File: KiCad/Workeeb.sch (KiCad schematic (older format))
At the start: 103 parts

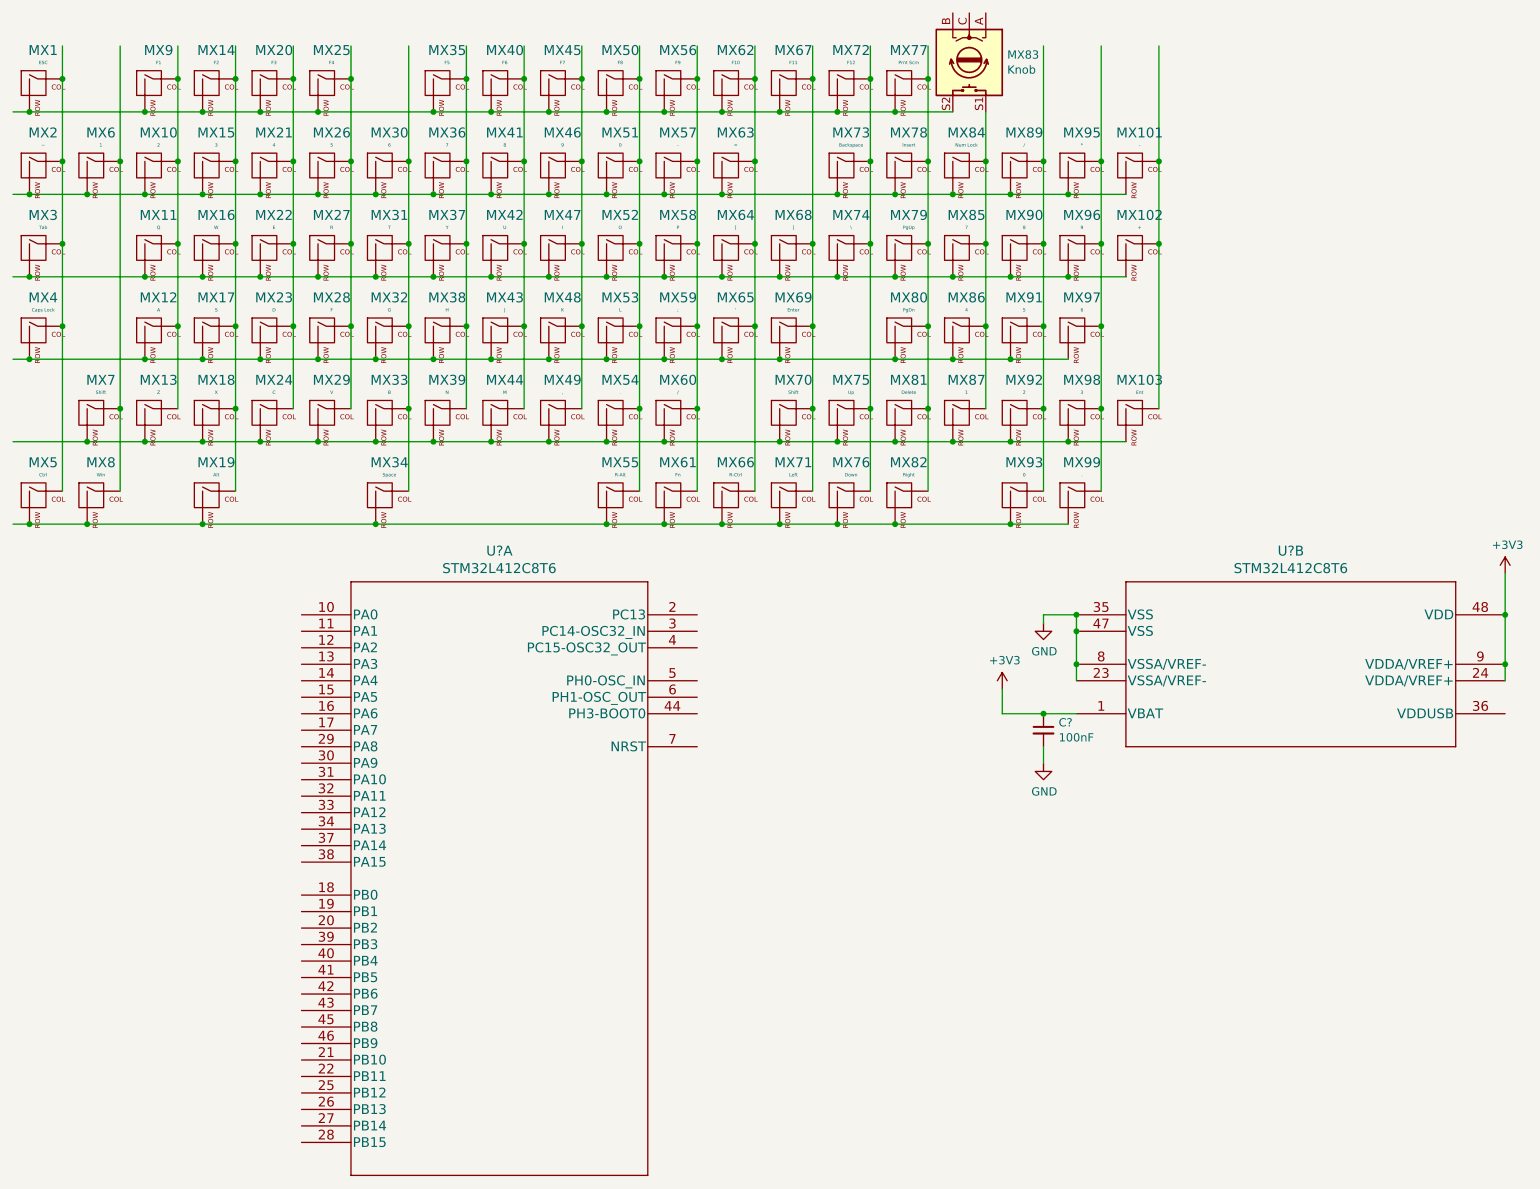
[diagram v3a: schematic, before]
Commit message: Place some things and rename some stuff
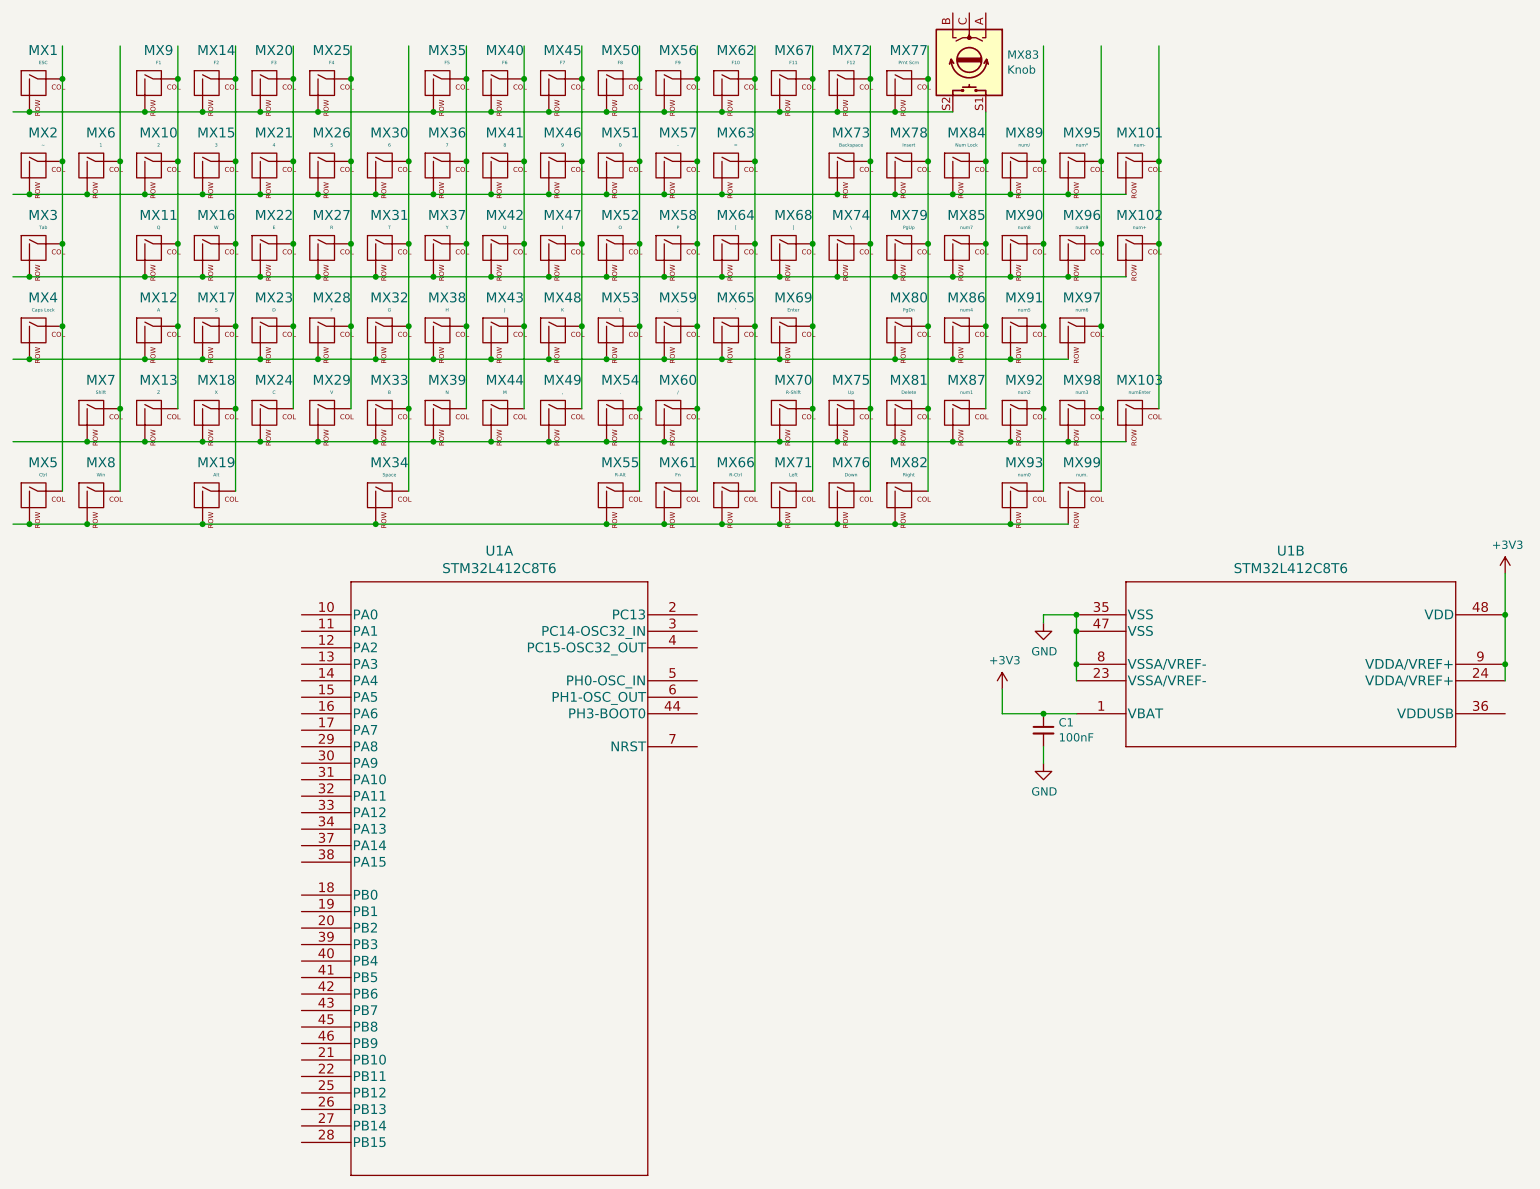
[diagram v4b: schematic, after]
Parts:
- C1: renamed from C?; footprint (none) -> Capacitor_SMD:C_0805_2012Metric
- MX101: value - -> num-
- MX102: value + -> num+
- MX103: value Ent -> numEnter
- MX70: value Shift -> R-Shift
- MX85: value 7 -> num7
- MX86: value 4 -> num4
- MX87: value 1 -> num1
- MX89: value / -> num/
- MX90: value 8 -> num8
- MX91: value 5 -> num5
- MX92: value 2 -> num2
- MX93: value 0 -> num0
- MX95: value * -> num*
- MX96: value 9 -> num9
- MX97: value 6 -> num6
- MX98: value 3 -> num3
- MX99: value . -> num.
- U1: renamed from U?; footprint LQFP-48 -> STM32L412C8T6:STM32L412C8T6
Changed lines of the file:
@@
-$EndComp
-$Comp
-L Workeeb-rescue:MX-NoLED-MX_Alps_Hybrid MX70
-U 1 1 61A3D951
-P 5450 3050
-F 0 "MX70" H 5483 3273 60  0000 C CNN
-F 1 "Shift" H 5483 3199 20  0000 C CNN
-F 2 "MX_Only:MXOnly-1.75U-NoLED" H 4825 3025 60  0001 C CNN
-F 3 "" H 4825 3025 60  0001 C CNN
-	1    5450 3050
-	1    0    0    -1
 $EndComp
 $Comp
@@
 P 6500 2050
 F 0 "MX85" H 6533 2273 60  0000 C CNN
-F 1 "7" H 6533 2199 20  0000 C CNN
+F 1 "num7" H 6533 2199 20  0000 C CNN
 F 2 "MX_Only:MXOnly-1U-NoLED" H 5875 2025 60  0001 C CNN
 F 3 "" H 5875 2025 60  0001 C CNN
 	1    6500 2050
-	1    0    0    -1
-$EndComp
-$Comp
-L Workeeb-rescue:MX-NoLED-MX_Alps_Hybrid MX86
-U 1 1 61A4EEF6
-P 6500 2550
-F 0 "MX86" H 6533 2773 60  0000 C CNN
-F 1 "4" H 6533 2699 20  0000 C CNN
-F 2 "MX_Only:MXOnly-1U-NoLED" H 5875 2525 60  0001 C CNN
-F 3 "" H 5875 2525 60  0001 C CNN
-	1    6500 2550
 	1    0    0    -1
 $EndComp
@@
 P 6500 3050
 F 0 "MX87" H 6533 3273 60  0000 C CNN
-F 1 "1" H 6533 3199 20  0000 C CNN
+F 1 "num1" H 6533 3199 20  0000 C CNN
 F 2 "MX_Only:MXOnly-1U-NoLED" H 5875 3025 60  0001 C CNN
 F 3 "" H 5875 3025 60  0001 C CNN
@@
 P 6850 1550
 F 0 "MX89" H 6883 1773 60  0000 C CNN
-F 1 "/" H 6883 1699 20  0000 C CNN
+F 1 "num/" H 6883 1699 20  0000 C CNN
 F 2 "MX_Only:MXOnly-1U-NoLED" H 6225 1525 60  0001 C CNN
 F 3 "" H 6225 1525 60  0001 C CNN
@@
 P 6850 2050
 F 0 "MX90" H 6883 2273 60  0000 C CNN
-F 1 "8" H 6883 2199 20  0000 C CNN
+F 1 "num8" H 6883 2199 20  0000 C CNN
 F 2 "MX_Only:MXOnly-1U-NoLED" H 6225 2025 60  0001 C CNN
 F 3 "" H 6225 2025 60  0001 C CNN
 	1    6850 2050
-	1    0    0    -1
-$EndComp
-$Comp
-L Workeeb-rescue:MX-NoLED-MX_Alps_Hybrid MX91
-U 1 1 61A511A4
-P 6850 2550
-F 0 "MX91" H 6883 2773 60  0000 C CNN
-F 1 "5" H 6883 2699 20  0000 C CNN
-F 2 "MX_Only:MXOnly-1U-NoLED" H 6225 2525 60  0001 C CNN
-F 3 "" H 6225 2525 60  0001 C CNN
-	1    6850 2550
 	1    0    0    -1
 $EndComp
@@
 P 6850 3050
 F 0 "MX92" H 6883 3273 60  0000 C CNN
-F 1 "2" H 6883 3199 20  0000 C CNN
+F 1 "num2" H 6883 3199 20  0000 C CNN
 F 2 "MX_Only:MXOnly-1U-NoLED" H 6225 3025 60  0001 C CNN
 F 3 "" H 6225 3025 60  0001 C CNN
@@
 P 6850 3550
 F 0 "MX93" H 6883 3773 60  0000 C CNN
-F 1 "0" H 6883 3699 20  0000 C CNN
+F 1 "num0" H 6883 3699 20  0000 C CNN
 F 2 "MX_Only:MXOnly-2U-NoLED" H 6225 3525 60  0001 C CNN
 F 3 "" H 6225 3525 60  0001 C CNN
@@
 P 7200 1550
 F 0 "MX95" H 7233 1773 60  0000 C CNN
-F 1 "*" H 7233 1699 20  0000 C CNN
+F 1 "num*" H 7233 1699 20  0000 C CNN
 F 2 "MX_Only:MXOnly-1U-NoLED" H 6575 1525 60  0001 C CNN
 F 3 "" H 6575 1525 60  0001 C CNN
@@
 P 7200 2050
 F 0 "MX96" H 7233 2273 60  0000 C CNN
-F 1 "9" H 7233 2199 20  0000 C CNN
+F 1 "num9" H 7233 2199 20  0000 C CNN
 F 2 "MX_Only:MXOnly-1U-NoLED" H 6575 2025 60  0001 C CNN
 F 3 "" H 6575 2025 60  0001 C CNN
@@
 P 7200 2550
 F 0 "MX97" H 7233 2773 60  0000 C CNN
-F 1 "6" H 7233 2699 20  0000 C CNN
+F 1 "num6" H 7233 2699 20  0000 C CNN
 F 2 "MX_Only:MXOnly-1U-NoLED" H 6575 2525 60  0001 C CNN
 F 3 "" H 6575 2525 60  0001 C CNN
@@
 P 7200 3050
 F 0 "MX98" H 7233 3273 60  0000 C CNN
-F 1 "3" H 7233 3199 20  0000 C CNN
+F 1 "num3" H 7233 3199 20  0000 C CNN
 F 2 "MX_Only:MXOnly-1U-NoLED" H 6575 3025 60  0001 C CNN
 F 3 "" H 6575 3025 60  0001 C CNN
@@
 P 7200 3550
 F 0 "MX99" H 7233 3773 60  0000 C CNN
-F 1 "." H 7233 3699 20  0000 C CNN
+F 1 "num." H 7233 3699 20  0000 C CNN
 F 2 "MX_Only:MXOnly-1U-NoLED" H 6575 3525 60  0001 C CNN
 F 3 "" H 6575 3525 60  0001 C CNN
@@
 P 7550 1550
 F 0 "MX101" H 7583 1773 60  0000 C CNN
-F 1 "-" H 7583 1699 20  0000 C CNN
+F 1 "num-" H 7583 1699 20  0000 C CNN
 F 2 "MX_Only:MXOnly-1U-NoLED" H 6925 1525 60  0001 C CNN
 F 3 "" H 6925 1525 60  0001 C CNN
@@
 P 7550 2050
 F 0 "MX102" H 7583 2273 60  0000 C CNN
-F 1 "+" H 7583 2199 20  0000 C CNN
+F 1 "num+" H 7583 2199 20  0000 C CNN
 F 2 "MX_Only:MXOnly-2U-NoLED" H 6925 2025 60  0001 C CNN
 F 3 "" H 6925 2025 60  0001 C CNN
@@
 P 7550 3050
 F 0 "MX103" H 7583 3273 60  0000 C CNN
-F 1 "Ent" H 7583 3199 20  0000 C CNN
+F 1 "numEnter" H 7583 3199 20  0000 C CNN
 F 2 "MX_Only:MXOnly-2U-NoLED" H 6925 3025 60  0001 C CNN
 F 3 "" H 6925 3025 60  0001 C CNN
@@
 	6650 1200 6650 1500
 $Comp
-L STM32L412C8T6:STM32L412C8T6 U?
+L STM32L412C8T6:STM32L412C8T6 U1
 U 1 1 6202699F
 P 2500 4250
-F 0 "U?" H 3700 4637 60  0000 C CNN
+F 0 "U1" H 3700 4637 60  0000 C CNN
 F 1 "STM32L412C8T6" H 3700 4531 60  0000 C CNN
-F 2 "LQFP-48" H 3700 4490 60  0001 C CNN
+F 2 "STM32L412C8T6:STM32L412C8T6" H 3700 4490 60  0001 C CNN
 F 3 "" H 2500 4250 60  0000 C CNN
 	1    2500 4250
@@
 $EndComp
 $Comp
-L STM32L412C8T6:STM32L412C8T6 U?
+L STM32L412C8T6:STM32L412C8T6 U1
 U 2 1 6203009A
 P 7200 4250
-F 0 "U?" H 8500 4637 60  0000 C CNN
+F 0 "U1" H 8500 4637 60  0000 C CNN
 F 1 "STM32L412C8T6" H 8500 4531 60  0000 C CNN
-F 2 "LQFP-48" H 8400 4490 60  0001 C CNN
+F 2 "STM32L412C8T6:STM32L412C8T6" H 8400 4490 60  0001 C CNN
 F 3 "" H 7200 4250 60  0000 C CNN
 	2    7200 4250
@@
 $EndComp
 $Comp
-L Device:C_Small C?
+L Device:C_Small C1
 U 1 1 6203DBCE
 P 7000 4950
-F 0 "C?" H 7092 4996 50  0000 L CNN
+F 0 "C1" H 7092 4996 50  0000 L CNN
 F 1 "100nF" H 7092 4905 50  0000 L CNN
-F 2 "" H 7000 4950 50  0001 C CNN
+F 2 "Capacitor_SMD:C_0805_2012Metric" H 7000 4950 50  0001 C CNN
 F 3 "~" H 7000 4950 50  0001 C CNN
 	1    7000 4950
@@
 	7000 5050 7000 5150
 $Comp
-L power:GND #PWR?
+L power:GND #PWR0101
 U 1 1 62054B6D
 P 7000 5150
-F 0 "#PWR?" H 7000 4900 50  0001 C CNN
+F 0 "#PWR0101" H 7000 4900 50  0001 C CNN
 F 1 "GND" H 7005 4977 50  0000 C CNN
 F 2 "" H 7000 5150 50  0001 C CNN
@@
 $EndComp
 $Comp
-L power:+3V3 #PWR?
+L power:+3V3 #PWR0102
 U 1 1 62063635
 P 9800 4000
-F 0 "#PWR?" H 9800 3850 50  0001 C CNN
+F 0 "#PWR0102" H 9800 3850 50  0001 C CNN
 F 1 "+3V3" H 9815 4173 50  0000 C CNN
 F 2 "" H 9800 4000 50  0001 C CNN
@@
 $EndComp
 $Comp
-L power:+3V3 #PWR?
+L power:+3V3 #PWR0103
 U 1 1 62064F17
 P 6750 4700
-F 0 "#PWR?" H 6750 4550 50  0001 C CNN
+F 0 "#PWR0103" H 6750 4550 50  0001 C CNN
 F 1 "+3V3" H 6765 4873 50  0000 C CNN
 F 2 "" H 6750 4700 50  0001 C CNN
@@
 	7200 4550 7200 4350
 $Comp
-L power:GND #PWR?
+L power:GND #PWR0104
 U 1 1 6209EDE2
 P 7000 4300
-F 0 "#PWR?" H 7000 4050 50  0001 C CNN
+F 0 "#PWR0104" H 7000 4050 50  0001 C CNN
 F 1 "GND" H 7005 4127 50  0000 C CNN
 F 2 "" H 7000 4300 50  0001 C CNN
@@
 	1    0    0    -1
 $EndComp
+$Comp
+L Workeeb-rescue:MX-NoLED-MX_Alps_Hybrid MX86
+U 1 1 61A4EEF6
+P 6500 2550
+F 0 "MX86" H 6533 2773 60  0000 C CNN
+F 1 "num4" H 6533 2699 20  0000 C CNN
+F 2 "MX_Only:MXOnly-1U-NoLED" H 5875 2525 60  0001 C CNN
+F 3 "" H 5875 2525 60  0001 C CNN
+	1    6500 2550
+	1    0    0    -1
+$EndComp
+$Comp
+L Workeeb-rescue:MX-NoLED-MX_Alps_Hybrid MX91
+U 1 1 61A511A4
+P 6850 2550
+F 0 "MX91" H 6883 2773 60  0000 C CNN
+F 1 "num5" H 6883 2699 20  0000 C CNN
+F 2 "MX_Only:MXOnly-1U-NoLED" H 6225 2525 60  0001 C CNN
+F 3 "" H 6225 2525 60  0001 C CNN
+	1    6850 2550
+	1    0    0    -1
+$EndComp
+$Comp
+L Workeeb-rescue:MX-NoLED-MX_Alps_Hybrid MX70
+U 1 1 61A3D951
+P 5450 3050
+F 0 "MX70" H 5483 3273 60  0000 C CNN
+F 1 "R-Shift" H 5483 3199 20  0000 C CNN
+F 2 "MX_Only:MXOnly-1.75U-NoLED" H 4825 3025 60  0001 C CNN
+F 3 "" H 4825 3025 60  0001 C CNN
+	1    5450 3050
+	1    0    0    -1
+$EndComp
